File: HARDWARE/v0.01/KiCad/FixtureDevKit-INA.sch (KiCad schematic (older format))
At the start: 42 parts, among them J17 INA_0, J18 INA_1, J19 INA, J20 INA_0, J21 INA1, J22 INA3, J23 INA0, J24 INA1, J25 INA_3, J26 INA_3, J27 INA_40, J28 INA_3, J29 INA3, J30 INA3, U1 INA219BIDCNT, U2 INA219BIDCNT, U3 INA219BIDCNT, U4 INA219BIDCNT

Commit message: adding some comments for Howie
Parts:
- J17, J20: value INA_0 -> INA_40
- J18: value INA_1 -> INA_41
- J21, J24: value INA1 -> INA_41
- J22: value INA3 -> INA
- J23: value INA0 -> INA_40
- J25: value INA_3 -> INA_42
- J26, J28: value INA_3 -> INA_43
- J27: value INA_40 -> INA_42
- J29: value INA3 -> INA_42
- J30: value INA3 -> INA_43
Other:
- note added: "INA_40\n"
- note added: "INA_41\n"
- note added: "INA_42"
- note added: "INA_43"
- note removed: "INA_0\n"
- note removed: "INA_1\n"
- note removed: "INA_2\n\n"
- note removed: "INA_3\n"
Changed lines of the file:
@@
 LIBS:contrib
 LIBS:valves
+LIBS:FDN337N
 LIBS:Fixture-Dev-Kit-cache
 EELAYER 25 0
@@
 $Descr A4 11693 8268
 encoding utf-8
-Sheet 3 9
+Sheet 3 10
 Title ""
 Date ""
@@
 P 2900 3050
 F 0 "J20" H 2900 3150 50  0000 C CNN
-F 1 "INA_0" H 2900 2850 50  0000 C CNN
+F 1 "INA_40" H 2900 2850 50  0000 C CNN
 F 2 "" H 2900 3050 50  0001 C CNN
 F 3 "" H 2900 3050 50  0001 C CNN
@@
 P 2000 2000
 F 0 "J17" H 2000 2200 50  0000 C CNN
-F 1 "INA_0" H 2000 1700 50  0000 C CNN
+F 1 "INA_40" H 2000 1700 50  0000 C CNN
 F 2 "" H 2000 2000 50  0001 C CNN
 F 3 "" H 2000 2000 50  0001 C CNN
@@
 P 2000 4350
 F 0 "J23" H 2000 4550 50  0000 C CNN
-F 1 "INA0" H 2000 4050 50  0000 C CNN
+F 1 "INA_40" H 2000 4050 50  0000 C CNN
 F 2 "" H 2000 4350 50  0001 C CNN
 F 3 "" H 2000 4350 50  0001 C CNN
@@
 	1900 3950 1900 4150
 Text Notes 650  1800 0    118  ~ 0
-INA_0\n
+INA_40\n
 Wire Notes Line
 	550  1550 550  4600
@@
 P 5750 3050
 F 0 "J21" H 5750 3150 50  0000 C CNN
-F 1 "INA1" H 5750 2850 50  0000 C CNN
+F 1 "INA_41" H 5750 2850 50  0000 C CNN
 F 2 "" H 5750 3050 50  0001 C CNN
 F 3 "" H 5750 3050 50  0001 C CNN
@@
 P 4850 2000
 F 0 "J18" H 4850 2200 50  0000 C CNN
-F 1 "INA_1" H 4850 1700 50  0000 C CNN
+F 1 "INA_41" H 4850 1700 50  0000 C CNN
 F 2 "" H 4850 2000 50  0001 C CNN
 F 3 "" H 4850 2000 50  0001 C CNN
@@
 P 4850 4350
 F 0 "J24" H 4850 4550 50  0000 C CNN
-F 1 "INA1" H 4850 4050 50  0000 C CNN
+F 1 "INA_41" H 4850 4050 50  0000 C CNN
 F 2 "" H 4850 4350 50  0001 C CNN
 F 3 "" H 4850 4350 50  0001 C CNN
@@
 	4750 3950 4750 4150
 Text Notes 3500 1800 0    118  ~ 0
-INA_1\n
+INA_41\n
 Wire Notes Line
 	3400 1550 3400 4600
@@
 P 2900 6150
 F 0 "J27" H 2900 6250 50  0000 C CNN
-F 1 "INA_40" H 2900 5950 50  0000 C CNN
+F 1 "INA_42" H 2900 5950 50  0000 C CNN
 F 2 "" H 2900 6150 50  0001 C CNN
 F 3 "" H 2900 6150 50  0001 C CNN
@@
 P 2000 5100
 F 0 "J25" H 2000 5300 50  0000 C CNN
-F 1 "INA_3" H 2000 4800 50  0000 C CNN
+F 1 "INA_42" H 2000 4800 50  0000 C CNN
 F 2 "" H 2000 5100 50  0001 C CNN
 F 3 "" H 2000 5100 50  0001 C CNN
@@
 P 2000 7450
 F 0 "J29" H 2000 7650 50  0000 C CNN
-F 1 "INA3" H 2000 7150 50  0000 C CNN
+F 1 "INA_42" H 2000 7150 50  0000 C CNN
 F 2 "" H 2000 7450 50  0001 C CNN
 F 3 "" H 2000 7450 50  0001 C CNN
@@
 Wire Wire Line
 	1900 7050 1900 7250
-Text Notes 650  5050 0    118  ~ 0
-INA_2\n\n
+Text Notes 650  4900 0    118  ~ 0
+INA_42
 Wire Notes Line
 	550  4650 550  7700
@@
 P 5750 6150
 F 0 "J28" H 5750 6250 50  0000 C CNN
-F 1 "INA_3" H 5750 5950 50  0000 C CNN
+F 1 "INA_43" H 5750 5950 50  0000 C CNN
 F 2 "" H 5750 6150 50  0001 C CNN
 F 3 "" H 5750 6150 50  0001 C CNN
@@
 P 4850 5100
 F 0 "J26" H 4850 5300 50  0000 C CNN
-F 1 "INA_3" H 4850 4800 50  0000 C CNN
+F 1 "INA_43" H 4850 4800 50  0000 C CNN
 F 2 "" H 4850 5100 50  0001 C CNN
 F 3 "" H 4850 5100 50  0001 C CNN
@@
 P 4850 7450
 F 0 "J30" H 4850 7650 50  0000 C CNN
-F 1 "INA3" H 4850 7150 50  0000 C CNN
+F 1 "INA_43" H 4850 7150 50  0000 C CNN
 F 2 "" H 4850 7450 50  0001 C CNN
 F 3 "" H 4850 7450 50  0001 C CNN
@@
 	4750 7050 4750 7250
 Text Notes 3500 4900 0    118  ~ 0
-INA_3\n
+INA_43
 Wire Notes Line
 	3400 4650 3400 7700
@@
 P 6800 3050
 F 0 "J22" H 6800 3250 50  0000 C CNN
-F 1 "INA3" H 6800 2750 50  0000 C CNN
+F 1 "INA" H 6800 2750 50  0000 C CNN
 F 2 "" H 6800 3050 50  0001 C CNN
 F 3 "" H 6800 3050 50  0001 C CNN

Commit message: updating the cover page
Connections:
- net SCL renamed I2C-SCK
- net SDA renamed I2C-SDA
- net VCC renamed C4-VCC-3V3
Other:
- note removed: "TO DO:\n- is it okay to have so many headers on the I2C lines?\n"
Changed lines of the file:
@@
 Wire Notes Line
 	6300 1900 7500 1900
-Text Notes -6800 1400 0    157  ~ 0
-TO DO:\n- is it okay to have so many headers on the I2C lines?\n
 $Comp
 L TEST TP?
@@
 	5450 6100 5450 6150
 Connection ~ 5450 6150
+Text HLabel 1300 950  0    60   BiDi ~ 0
+I2C-SDA
+Text HLabel 1300 1100 0    60   BiDi ~ 0
+I2C-SCK
+Text HLabel 1300 1250 0    60   Input ~ 0
+C4-VCC-3V3
+Text Label 1450 950  0    60   ~ 0
+SDA
+Text Label 1450 1100 0    60   ~ 0
+SCL
+Wire Wire Line
+	1300 950  1450 950
+Wire Wire Line
+	1300 1100 1450 1100
+Wire Wire Line
+	1450 1250 1300 1250
+Text Label 1450 1250 0    60   ~ 0
+VCC
 $EndSCHEMATC

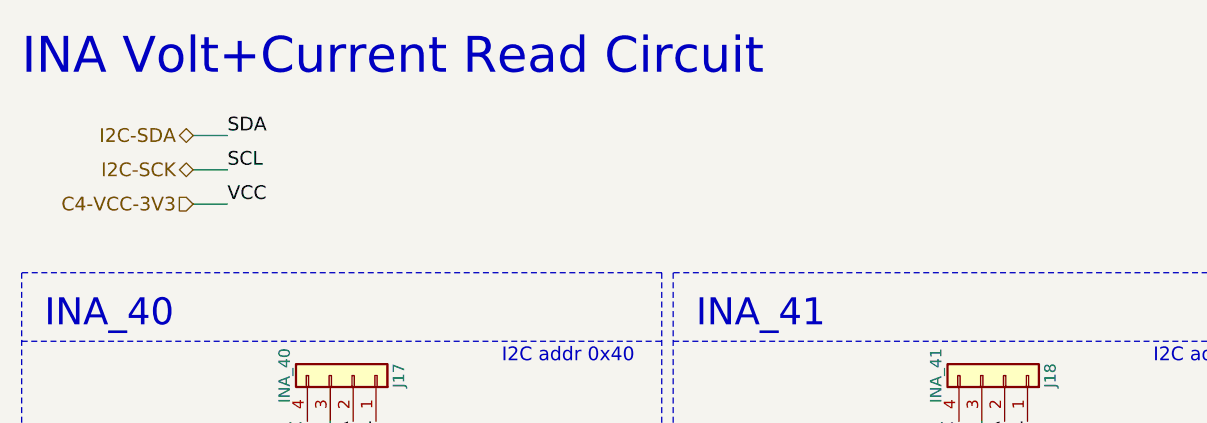
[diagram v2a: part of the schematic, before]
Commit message: adding labelings, hierarchy pins, and page titles
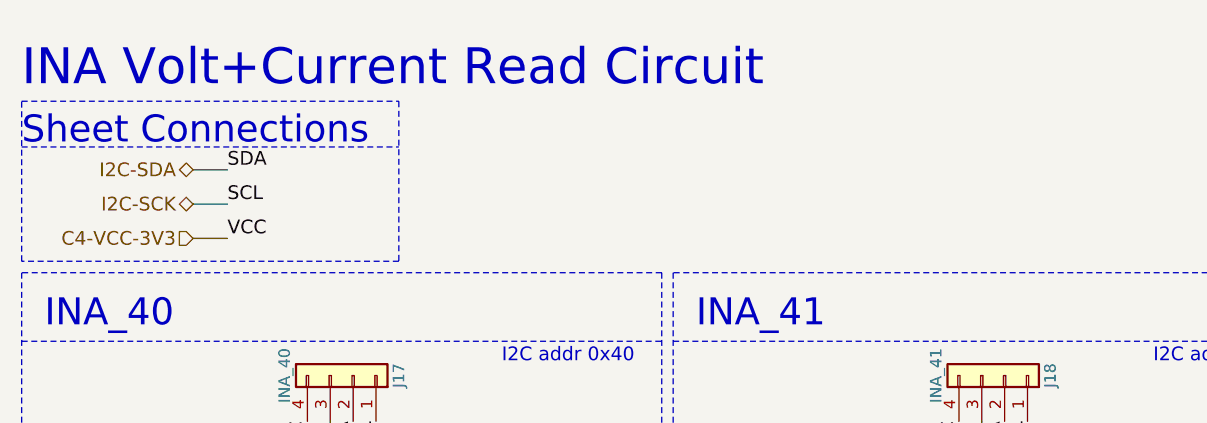
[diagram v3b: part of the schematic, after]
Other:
- note added: "Sheet Connections"
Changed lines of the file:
@@
 encoding utf-8
 Sheet 3 10
-Title ""
-Date ""
-Rev ""
-Comp ""
-Comment1 ""
+Title "INA Circuits"
+Date "2017-10-25"
+Rev "v0.01"
+Comp "Next Thing Co"
+Comment1 "Havin' a Blast!"
 Comment2 ""
 Comment3 ""
 Comment4 ""
 $EndDescr
-Text Notes 550  700  0    157  ~ 0
+Text Notes 550  750  0    157  ~ 0
 INA Volt+Current Read Circuit\n
 $Comp
@@
 	5450 6100 5450 6150
 Connection ~ 5450 6150
-Text HLabel 1300 950  0    60   BiDi ~ 0
+Text HLabel 1300 1100 0    60   BiDi ~ 0
 I2C-SDA
-Text HLabel 1300 1100 0    60   BiDi ~ 0
+Text HLabel 1300 1250 0    60   BiDi ~ 0
 I2C-SCK
-Text HLabel 1300 1250 0    60   Input ~ 0
+Text HLabel 1300 1400 0    60   Input ~ 0
 C4-VCC-3V3
-Text Label 1450 950  0    60   ~ 0
-SDA
 Text Label 1450 1100 0    60   ~ 0
-SCL
-Wire Wire Line
-	1300 950  1450 950
+SDA
+Text Label 1450 1250 0    60   ~ 0
+SCL
 Wire Wire Line
 	1300 1100 1450 1100
 Wire Wire Line
-	1450 1250 1300 1250
-Text Label 1450 1250 0    60   ~ 0
-VCC
+	1300 1250 1450 1250
+Wire Wire Line
+	1450 1400 1300 1400
+Text Label 1450 1400 0    60   ~ 0
+VCC
+Text Notes 550  1000 0    118  ~ 0
+Sheet Connections
+Wire Notes Line
+	550  800  2200 800
+Wire Notes Line
+	2200 800  2200 1500
+Wire Notes Line
+	2200 1500 550  1500
+Wire Notes Line
+	550  1500 550  800
+Wire Notes Line
+	550  1000 2200 1000
 $EndSCHEMATC

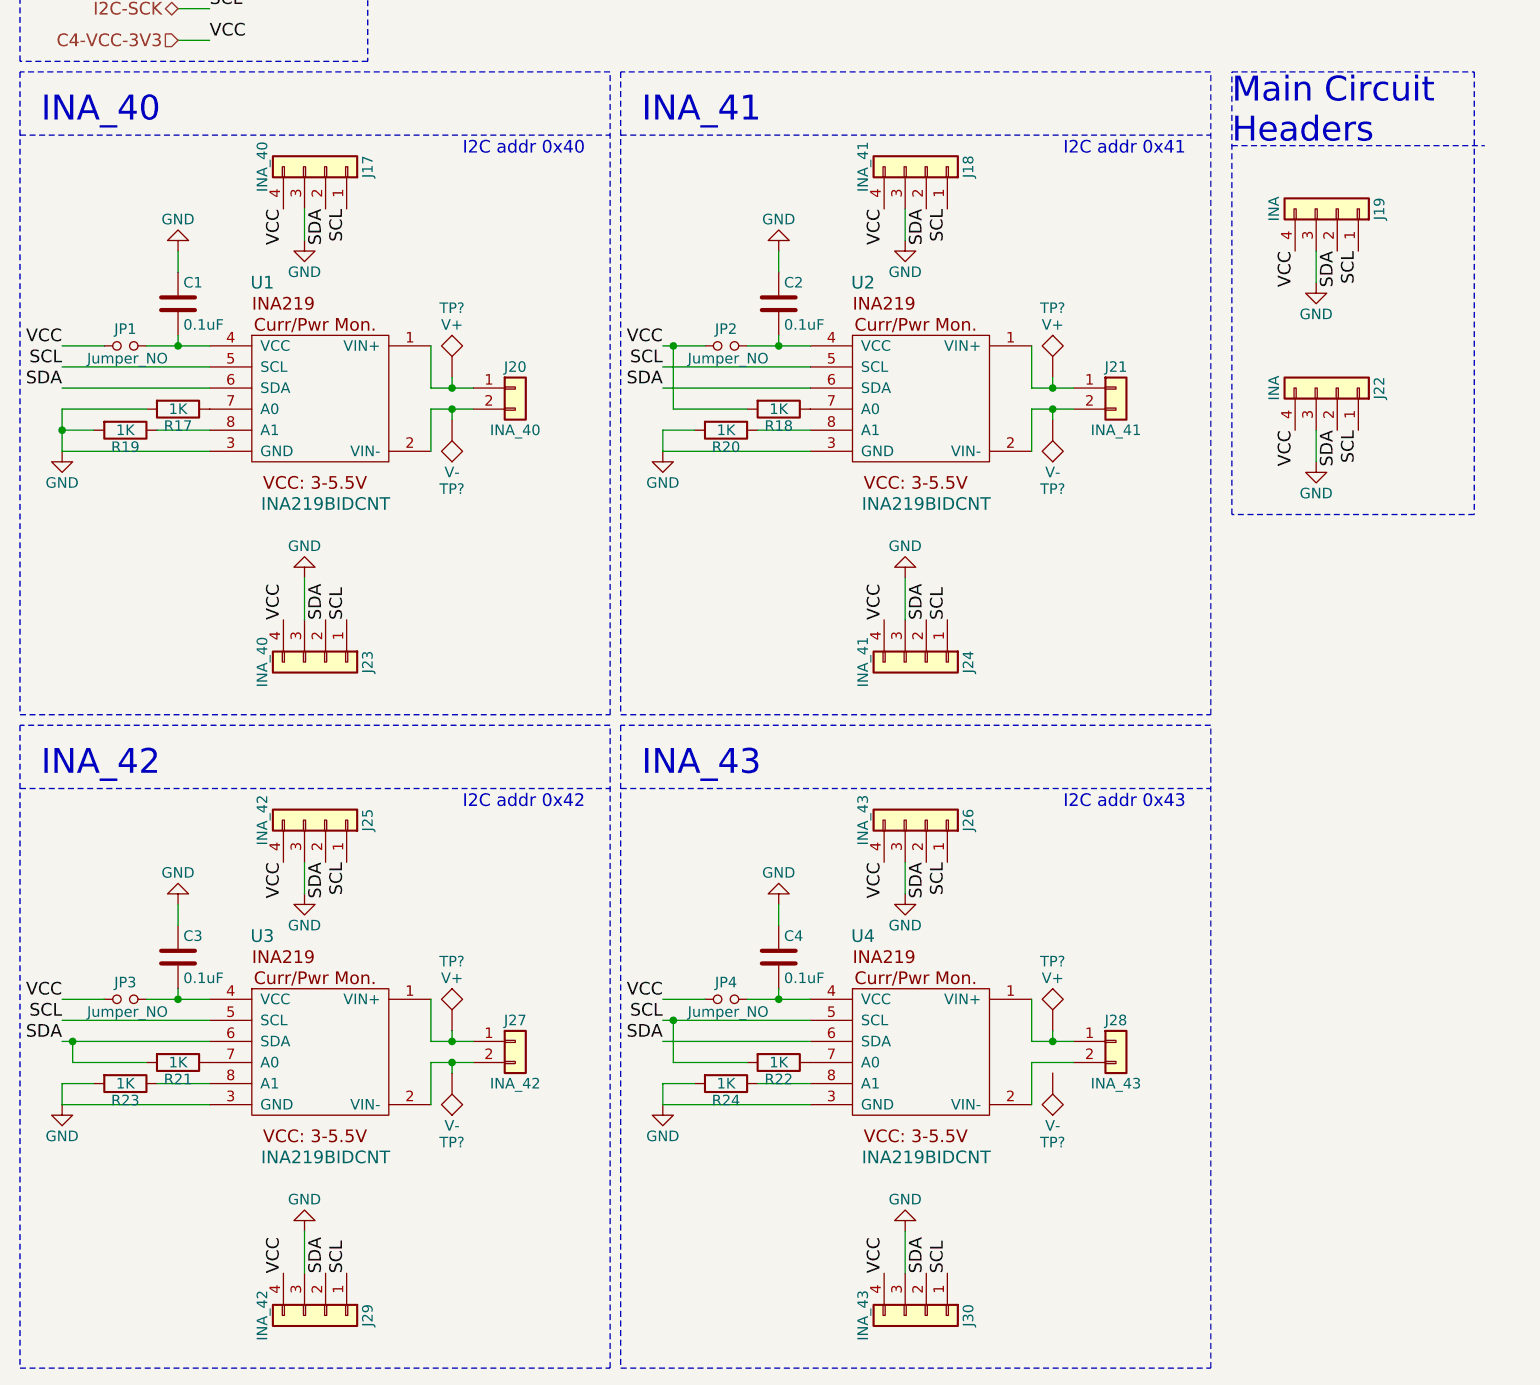
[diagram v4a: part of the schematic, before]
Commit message: cleaning up schematic, run rules check, generate net list
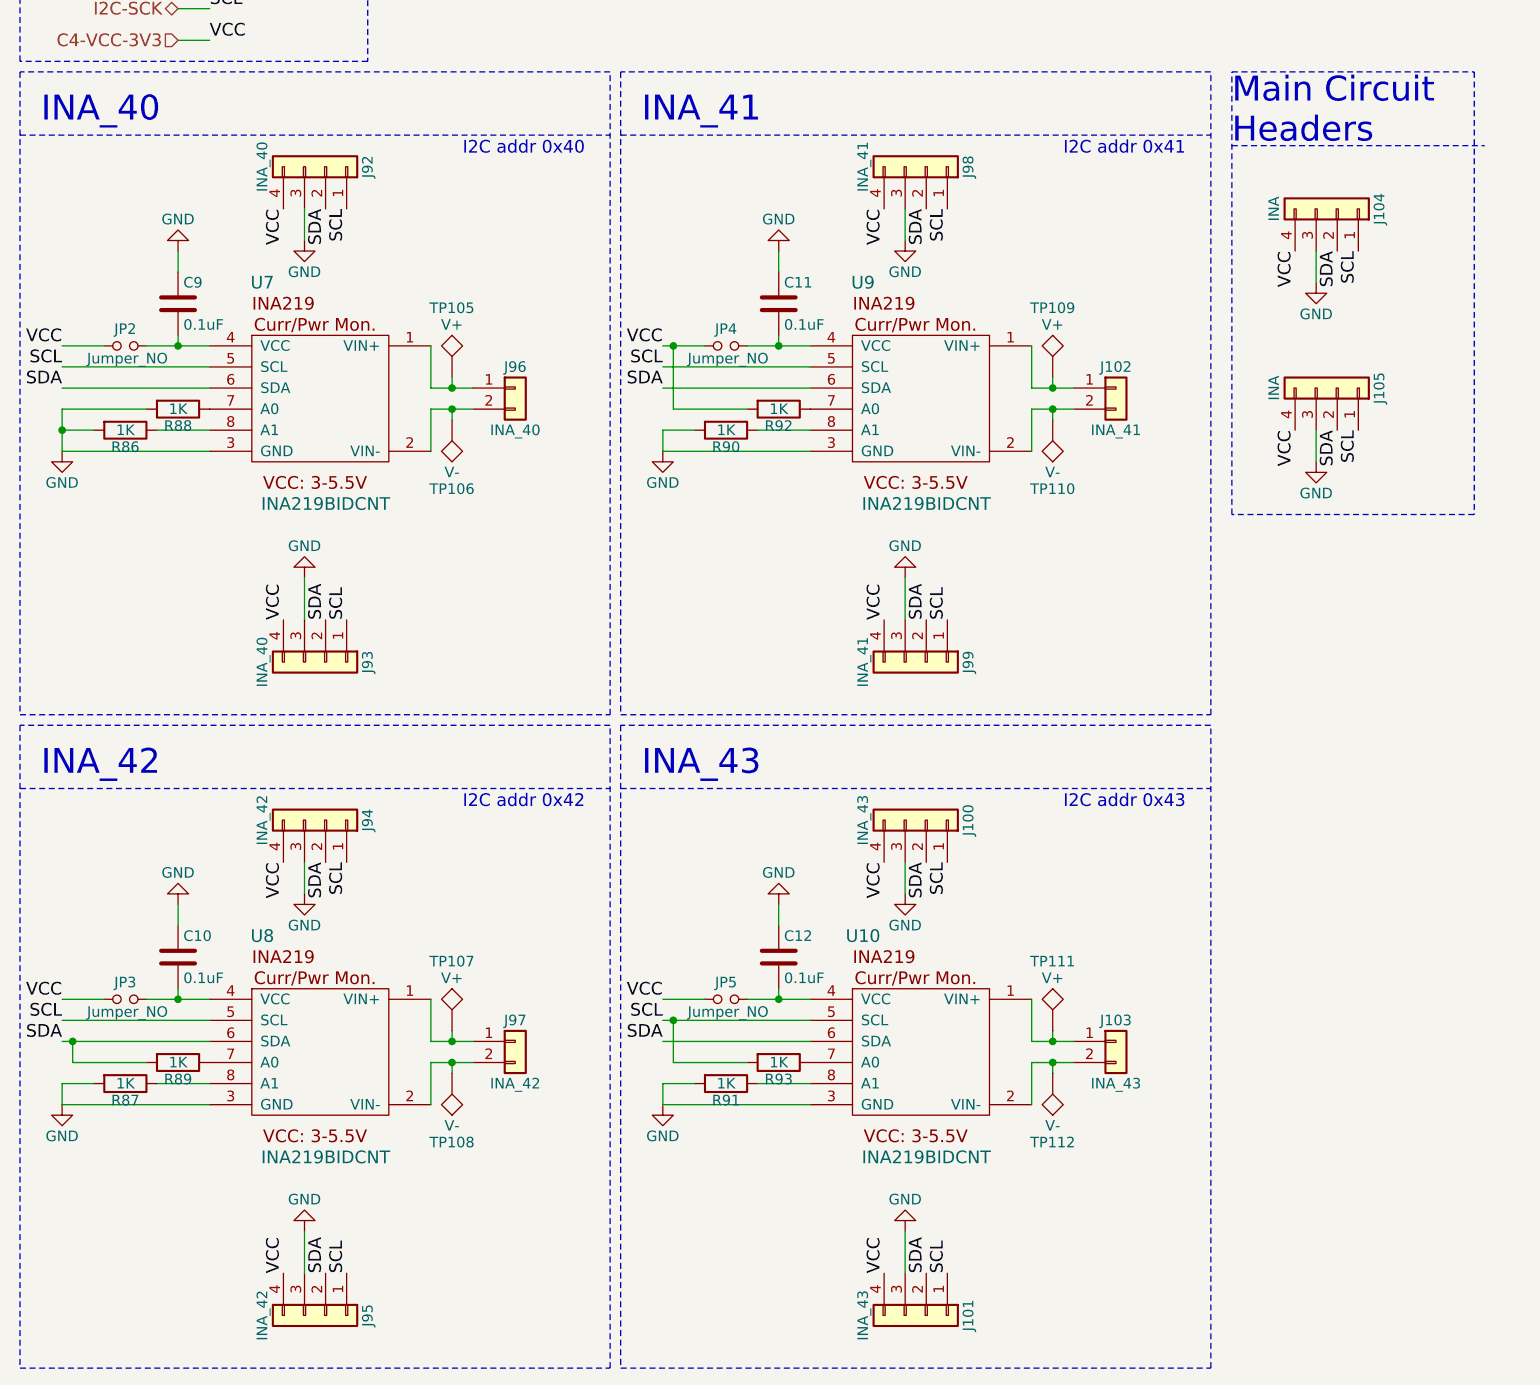
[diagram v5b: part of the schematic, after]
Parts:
- gave numbers to parts that had none: 8
- renumbered C3 to C10, C2 to C11, C4 to C12, C1 to C9, J26 to J100, J30 to J101, J21 to J102, J28 to J103, J19 to J104, J22 to J105, J17 to J92, J23 to J93, J25 to J94, J29 to J95, J20 to J96, J27 to J97, J18 to J98, J24 to J99, JP1 to JP2, JP2 to JP4, JP4 to JP5, R19 to R86, R23 to R87, R17 to R88, R21 to R89, R20 to R90, R24 to R91, R18 to R92, R22 to R93, U4 to U10, U1 to U7, U3 to U8, U2 to U9
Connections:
- net at J103.2 (Pin_2), U10.2 (VIN-): now also TP112.1
